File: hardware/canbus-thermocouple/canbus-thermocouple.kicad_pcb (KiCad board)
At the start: 4 copper layers, 55 x 35 mm, 34 parts, among them J1 USB_B_Micro, J2 UART, J3 10k NTC, J4 CANBus, J5 CANBus, J6 SWD, Q1 2N7002, Q2 2N7002, U1 MCP1754S-3302xCB, U2 STM32F042F6Px, U3 Voltage Regulator, U4 MCP2562HD

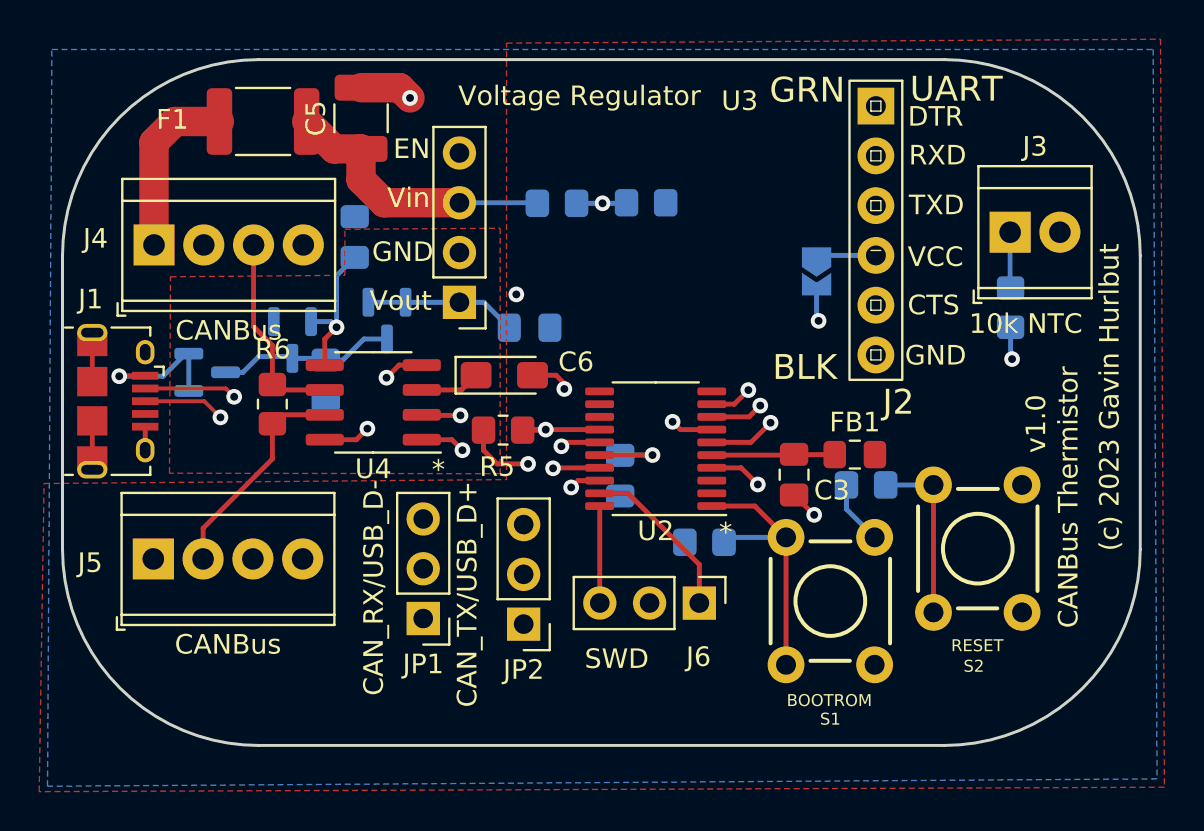
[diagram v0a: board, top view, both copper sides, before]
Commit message: Updated the thermocouple board, added OSHW to bottom of all boards
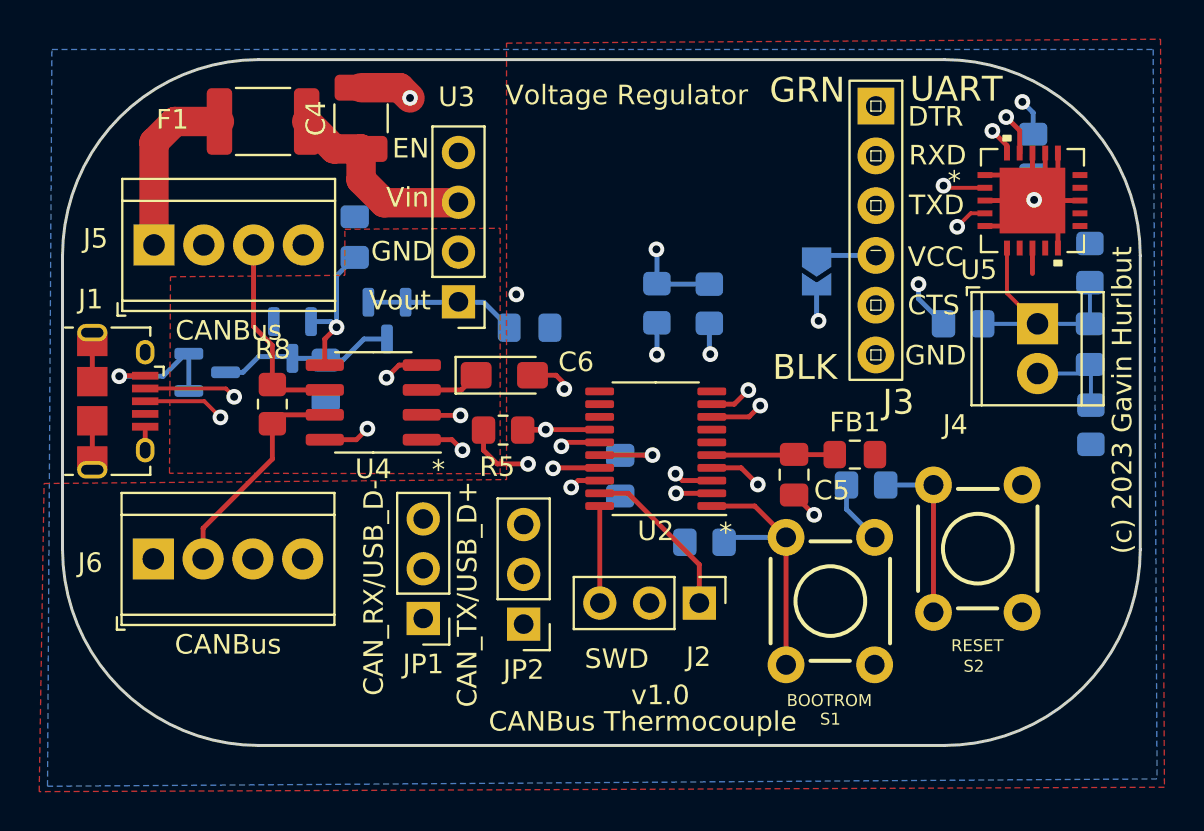
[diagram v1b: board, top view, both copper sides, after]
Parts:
- removed the J3 at (103.3, 77.4)
- added C8: 100nF, Capacitor_SMD:C_0805_2012Metric_Pad1.18x1.45mm_HandSolder, B.Cu at (107.4, 83.1)
- added C9: 100nF, Capacitor_SMD:C_0805_2012Metric_Pad1.18x1.45mm_HandSolder, B.Cu at (104.5, 73.5)
- added J4: K-Type, TerminalBlock_TE-Connectivity:TerminalBlock_TE_282834-2_1x02_P2.54mm_Horizontal, F.Cu at (104.8, 82.1)
- added R6: 2M, Resistor_SMD:R_0805_2012Metric_Pad1.20x1.40mm_HandSolder, B.Cu at (107.5, 87.2)
- added R9: 10k, Resistor_SMD:R_0805_2012Metric_Pad1.20x1.40mm_HandSolder, B.Cu at (85.3, 81.0)
- added REF**: OSHW-Logo2_7.3x6mm_SilkScreen, Symbol:OSHW-Logo2_7.3x6mm_SilkScreen, B.Cu at (80.8, 74.7)
- added U5: MCP96L01T-E/MX, UltraLibrarian:MCP96L01T-E&slash_MX, F.Cu at (104.5, 75.8)
- R3: value 499k 1% -> 1M
- R4: value 100k 1% -> 2M
- moved R4 22.9 mm to (107.4, 79.0), turned to 90 degrees
- moved R3 21.6 mm to (101.0, 82.1)
- moved R7 15.4 mm to (88.0, 81.1), turned to -90 degrees
- moved U3 0.06 mm to (75.2, 81.1)
- renumbered C2 to C1, C1 to C2, C4 to C3, C5 to C4, C3 to C5, J6 to J2, J2 to J3, J4 to J5, J5 to J6, R6 to R8
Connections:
- R3 pad 1: +12V -> +3V3
- R3 pad 2: VBAT_MON -> VIN+
- R4 pad 1: VBAT_MON -> VIN+
- R7 pad 2: VTHERM -> SDA
- U2 pad 10: ~{SPI1_SS} -> unconnected-(U2-Pad10)
- U2 pad 11: SPI1_SCK -> unconnected-(U2-Pad11)
- U2 pad 12: SPI1_MISO -> unconnected-(U2-Pad12)
- U2 pad 13: SPI1_MOSI -> unconnected-(U2-Pad13)
- U2 pad 2: SDA1 -> SDA
- U2 pad 3: SCL1 -> SCL
- U2 pad 6: VTHERM -> unconnected-(U2-Pad6)
- U2 pad 7: VBAT_MON -> unconnected-(U2-Pad7)
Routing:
- net SCL: track 0.00 -> 37.6 mm, vias 0 -> 3
- net SDA: track 0.00 -> 33.6 mm, vias 0 -> 3
- net VTHERM: track 25.1 -> 0.00 mm, vias 1 -> 0
- net VIN+: track 0.00 -> 24.4 mm, vias 0 -> 1
- net GND: track 16.5 -> 38.2 mm, vias 5 -> 6
- net VBAT_MON: track 17.4 -> 0.00 mm, vias 2 -> 0
- net VIN-: track 0.00 -> 17.1 mm, vias 0 -> 1
- net +3V3: track 22.3 -> 30.8 mm, vias 6 -> 8
- net +12V: track 14.4 -> 10.4 mm
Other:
- board text added: "CANBus Thermocouple"
- board text removed: "CANBus Thermistor"
